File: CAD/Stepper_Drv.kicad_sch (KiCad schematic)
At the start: 16 parts, among them U1 SN74F125DR, U2 SN74F125DR, U21 SN74F125DR, U22 SN74F125DR, U6 SN74F125DR

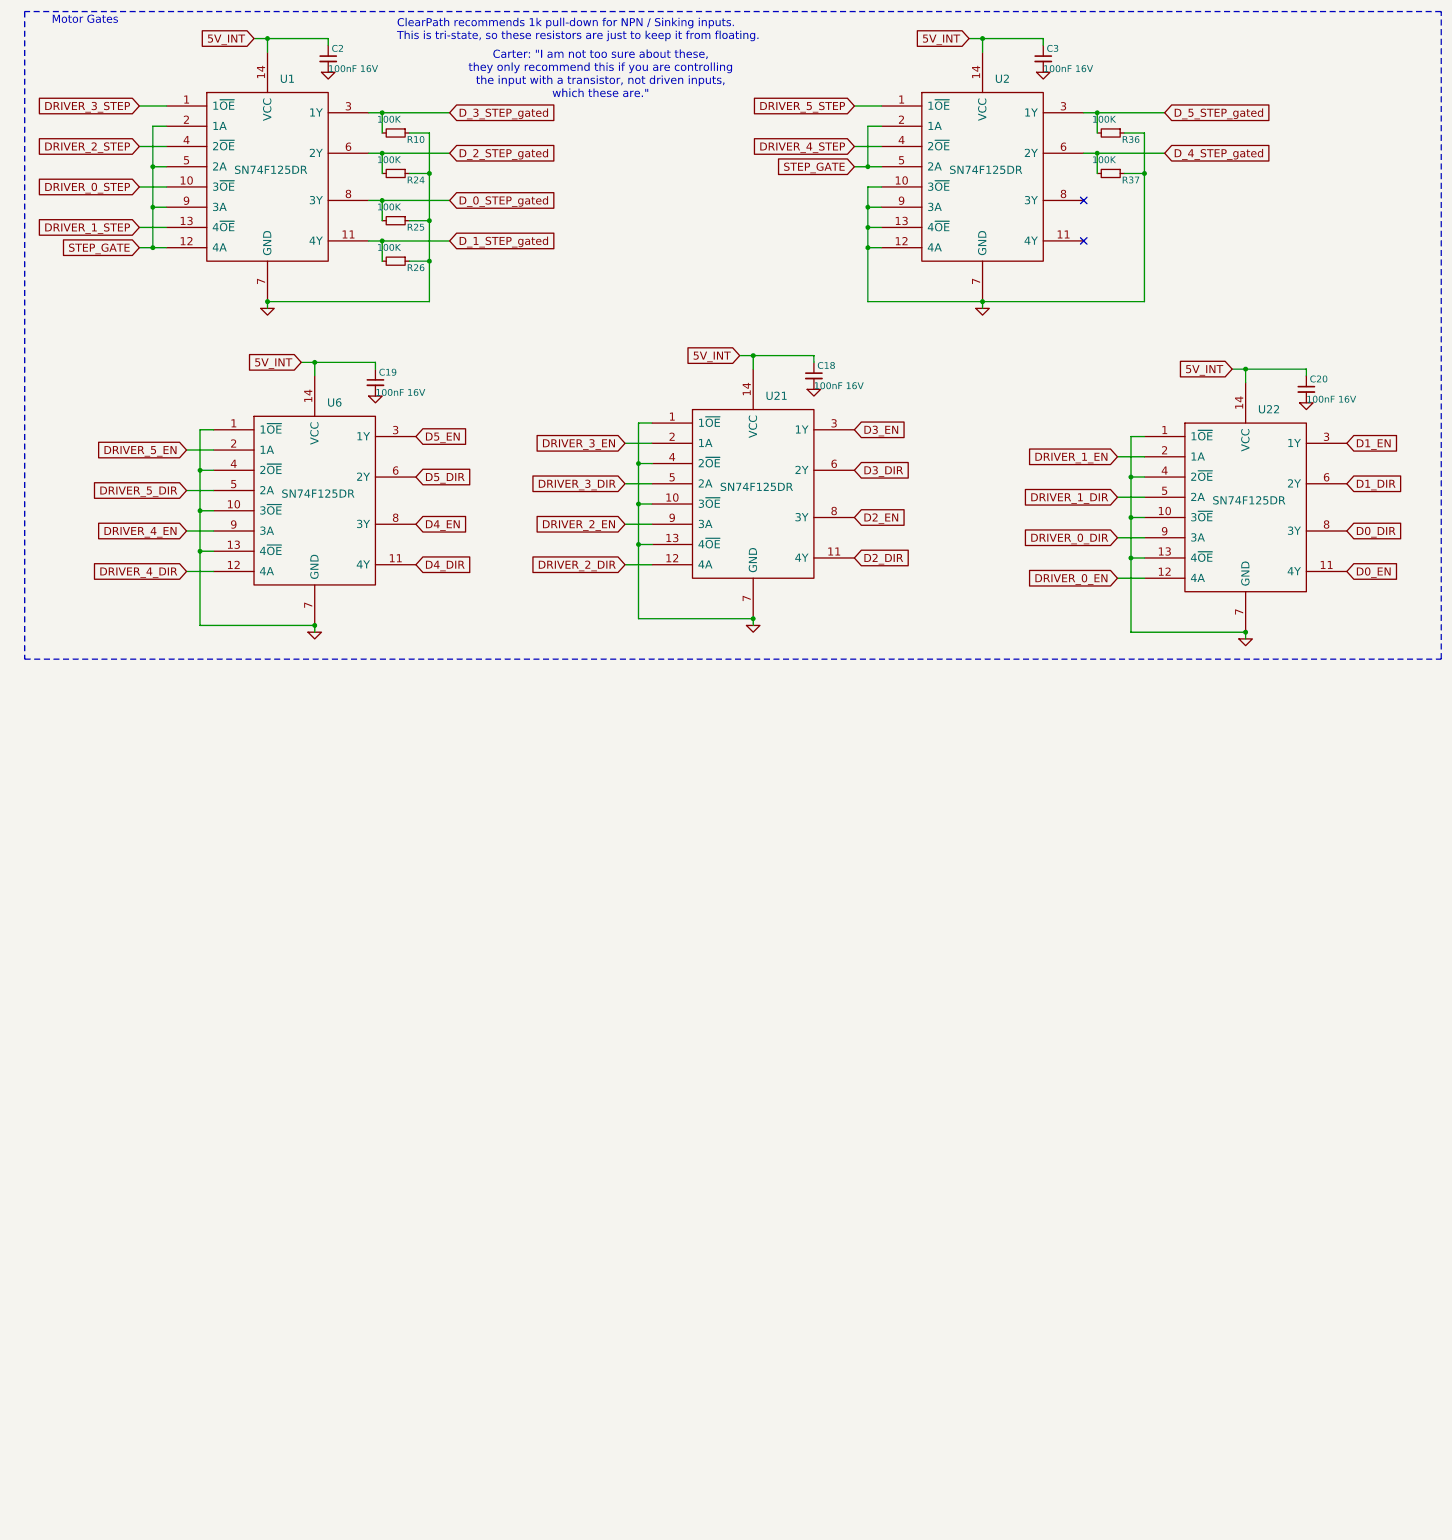
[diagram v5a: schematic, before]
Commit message: Started SN74LVC4245APWR
This chip is a dedicated 3v3-5v converter, 24 mA output
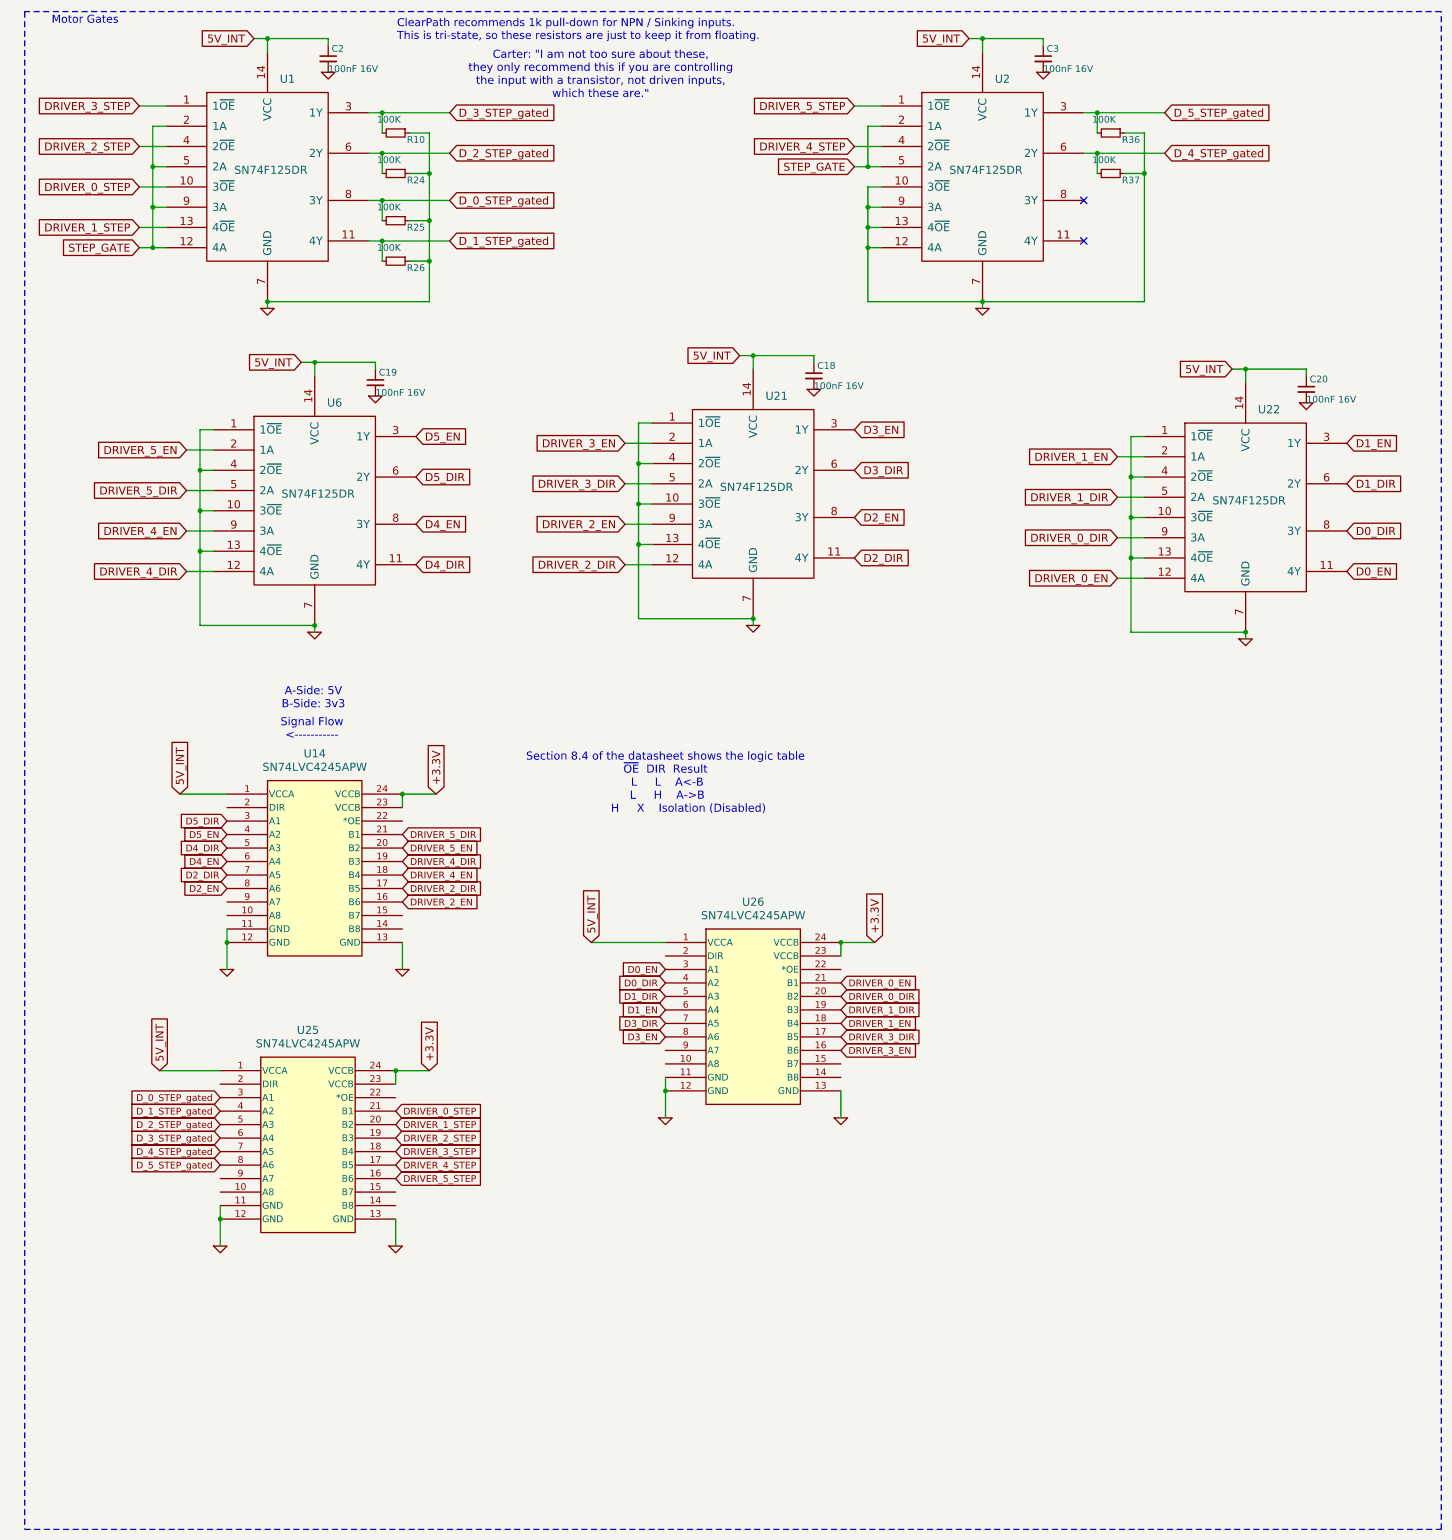
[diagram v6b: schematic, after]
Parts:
- added U14, U25, U26: SN74LVC4245APW, 3DPotter:PW24, symbol 3DPotter:SN74LVC4245APW
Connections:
- net 5V_INT: now also U14.1 (VCCA), U25.1 (VCCA), U26.1 (VCCA)
- net D0_DIR: now also U26.4 (A2)
- net D0_EN: now also U26.3 (A1)
- net D1_DIR: now also U26.5 (A3)
- net D1_EN: now also U26.6 (A4)
- net D2_DIR: now also U14.7 (A5)
- net D2_EN: now also U14.8 (A6)
- net D3_DIR: now also U26.7 (A5)
- net D3_EN: now also U26.8 (A6)
- net D4_DIR: now also U14.5 (A3)
- net D4_EN: now also U14.6 (A4)
- net D5_DIR: now also U14.3 (A1)
- net D5_EN: now also U14.4 (A2)
- net DRIVER_0_DIR: now also U26.20 (B2)
- net DRIVER_0_EN: now also U26.21 (B1)
- net DRIVER_0_STEP: now also U25.21 (B1)
- net DRIVER_1_DIR: now also U26.19 (B3)
- net DRIVER_1_EN: now also U26.18 (B4)
- net DRIVER_1_STEP: now also U25.20 (B2)
- net DRIVER_2_DIR: now also U14.17 (B5)
- net DRIVER_2_EN: now also U14.16 (B6)
- net DRIVER_2_STEP: now also U25.19 (B3)
- net DRIVER_3_DIR: now also U26.17 (B5)
- net DRIVER_3_EN: now also U26.16 (B6)
- net DRIVER_3_STEP: now also U25.18 (B4)
- net DRIVER_4_DIR: now also U14.19 (B3)
- net DRIVER_4_EN: now also U14.18 (B4)
- net DRIVER_4_STEP: now also U25.17 (B5)
- net DRIVER_5_DIR: now also U14.21 (B1)
- net DRIVER_5_EN: now also U14.20 (B2)
- net DRIVER_5_STEP: now also U25.16 (B6)
- net D_0_STEP_gated: now also U25.3 (A1)
- net D_1_STEP_gated: now also U25.4 (A2)
- net D_2_STEP_gated: now also U25.5 (A3)
- net D_3_STEP_gated: now also U25.6 (A4)
- net D_4_STEP_gated: now also U25.7 (A5)
- net D_5_STEP_gated: now also U25.8 (A6)
- net GND: now also U14.11 (GND), U14.12 (GND), U14.13 (GND), U25.11 (GND), U25.12 (GND), U25.13 (GND), U26.11 (GND), U26.12 (GND), U26.13 (GND)
- new net +3.3V: U14.23 (VCCB), U14.24 (VCCB), U25.23 (VCCB), U25.24 (VCCB), U26.23 (VCCB), U26.24 (VCCB)
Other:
- note added: "A-Side: 5V B-Side: 3v3"
- note added: "Section 8.4 of the datasheet shows the logic table ~{OE} DIR Result L L A<-B L H A->B H X Isolation (Disabled)"
- note added: "Signal Flow <-----------"

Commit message: Finish SN74LVC4245APWR schematic
Also adds a new pin to the mcu, "EN_DIR_GATE" serves same function as "STEP_GATE" this is necessary for the SN74LVC to power up safely. Pin is driven low to enable the device.
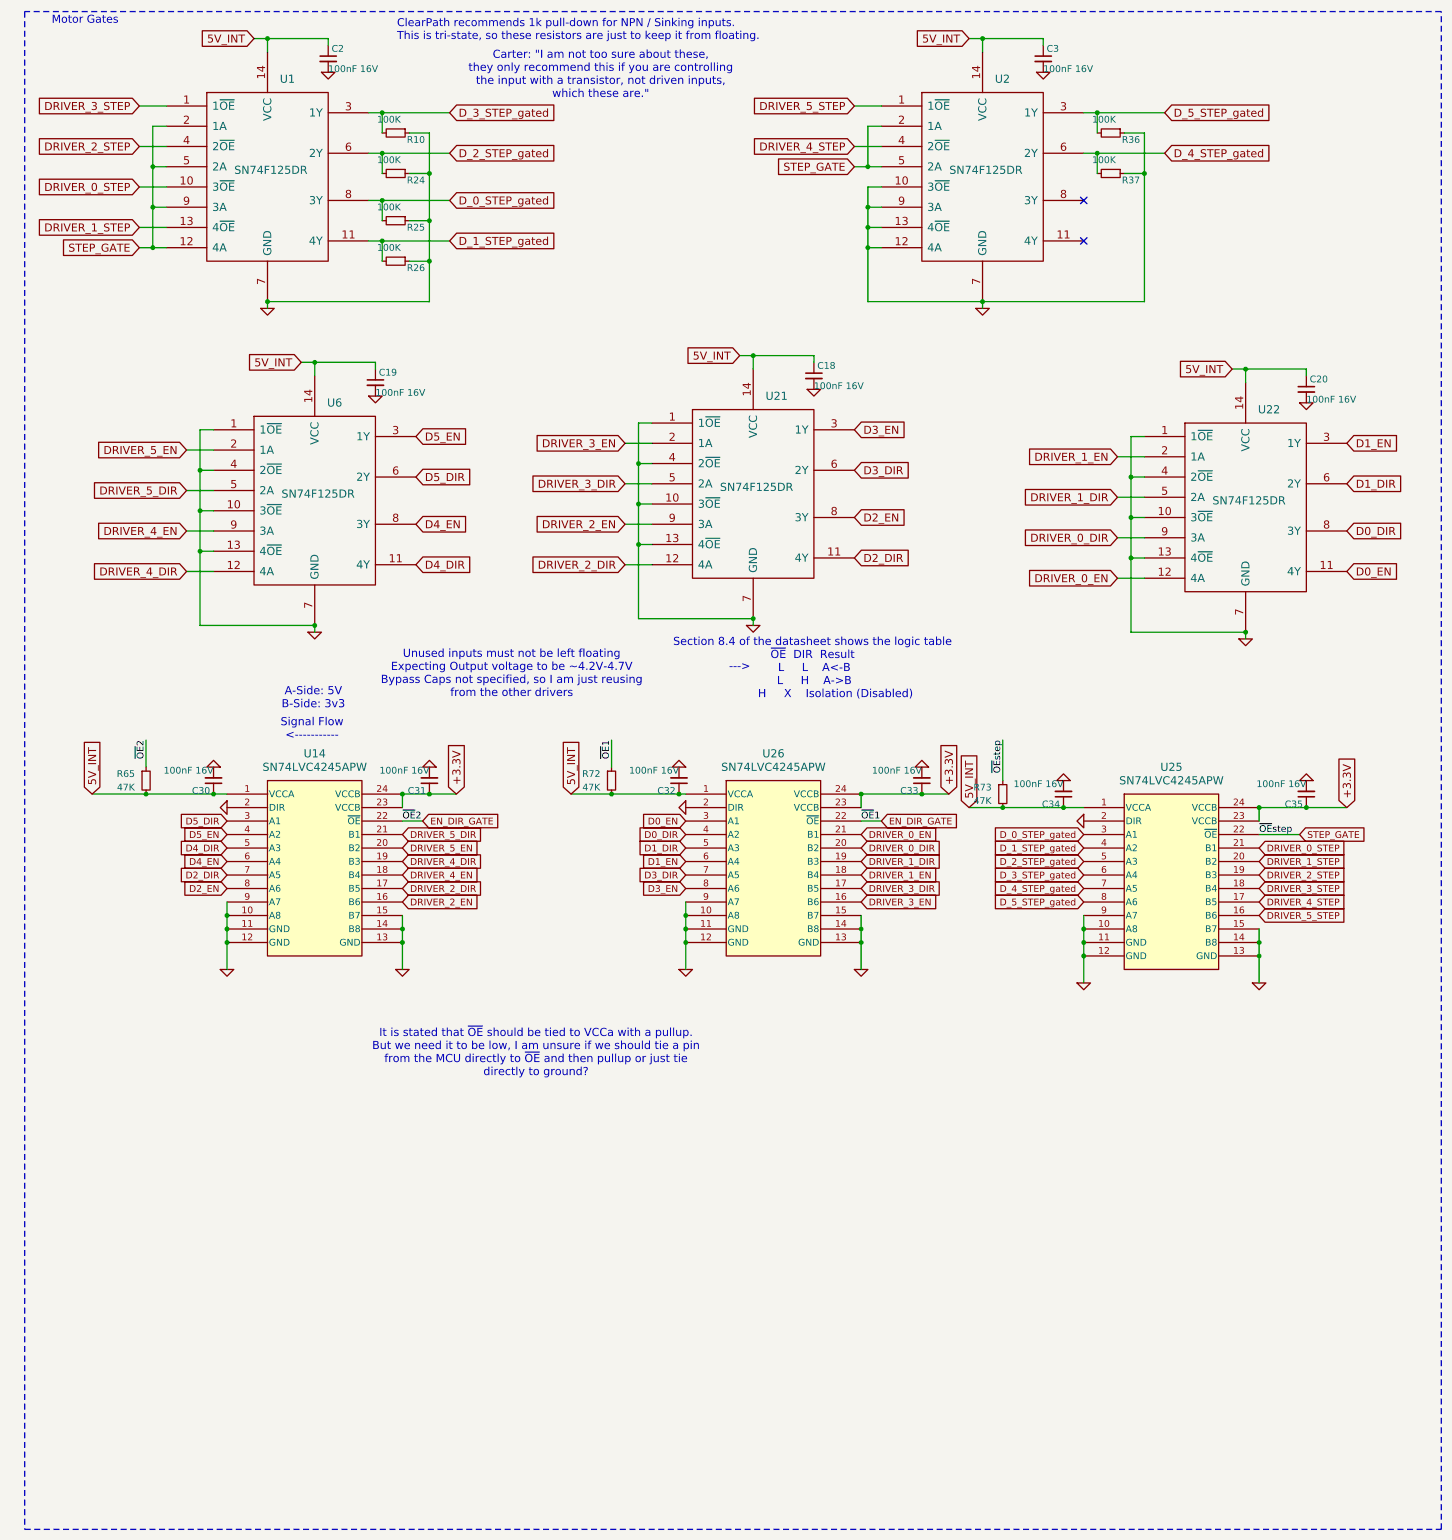
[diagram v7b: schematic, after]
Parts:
- added C30, C31, C32, C33, C34, C35: 100nF 16V, Capacitor_SMD:C_0402_1005Metric, symbol Device:C_Small
- added R65, R72, R73: 47K, Resistor_SMD:R_0402_1005Metric_Wbry, symbol Device:R_Small
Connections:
- net +3.3V: now also C31.1, C33.1, C35.1
- net 5V_INT: now also C30.1, C32.1, C34.1, R65.2, R72.2, R73.2
- net GND: now also U14.10 (A8), U14.14 (B8), U14.15 (B7), U14.2 (DIR), U14.9 (A7), U25.10 (A8), U25.14 (B8), U25.15 (B7), U25.2 (DIR), U25.9 (A7), U26.10 (A8), U26.14 (B8), U26.15 (B7), U26.2 (DIR), U26.9 (A7), C30.2, C31.2, C32.2, C33.2, C34.2, C35.2
- net STEP_GATE: now also U25.22 (~{OE}), R73.1
- net EN_DIR_GATE: now reaches U26.22 (~{OE})
- net EN_DIR_GATE: now also U14.22 (~{OE}), R65.1, R72.1
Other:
- note added: "--->"
- note added: "It is stated that ~{OE} should be tied to VCCa with a pullup. But we need it to be low, I am unsure if we should tie a pin from the MCU directly to ~{OE} and then pullup or just tie directly to ground?"
- note added: "Unused inputs must not be left floating Expecting Output voltage to be ~4.2V-4.7V Bypass Caps not specified, so I am just reusing from the other drivers"
- moved on the sheet: U25, U26

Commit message: 12 Unconnected left
Almost done :) Brian fried
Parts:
- C18, C19, C2, C20, C3, R10, R24, R25, R26, R36, R37, U1, U2, U21, U22, U6: now not fitted; now left out of the parts list
- R65, R72, R73: footprint Resistor_SMD:R_0402_1005Metric_Wbry -> Resistor_SMD:R_0402_1005Metric
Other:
- moved on the sheet: C30, C31, C32, C33, C34, C35, R65, R72, R73, U14, U25, U26
